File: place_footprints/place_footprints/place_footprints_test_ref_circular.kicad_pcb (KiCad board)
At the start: 2 copper layers, 64 parts

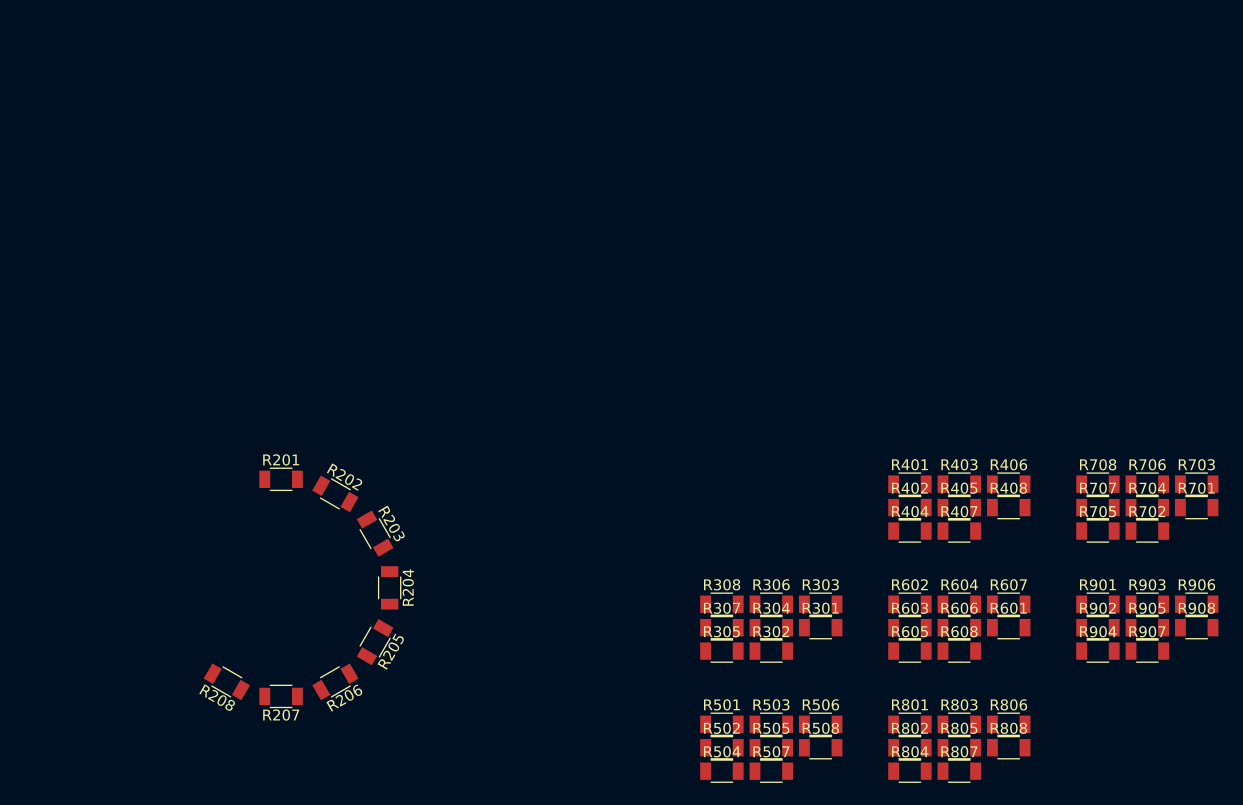
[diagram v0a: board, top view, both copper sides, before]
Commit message: Fixed circular placement
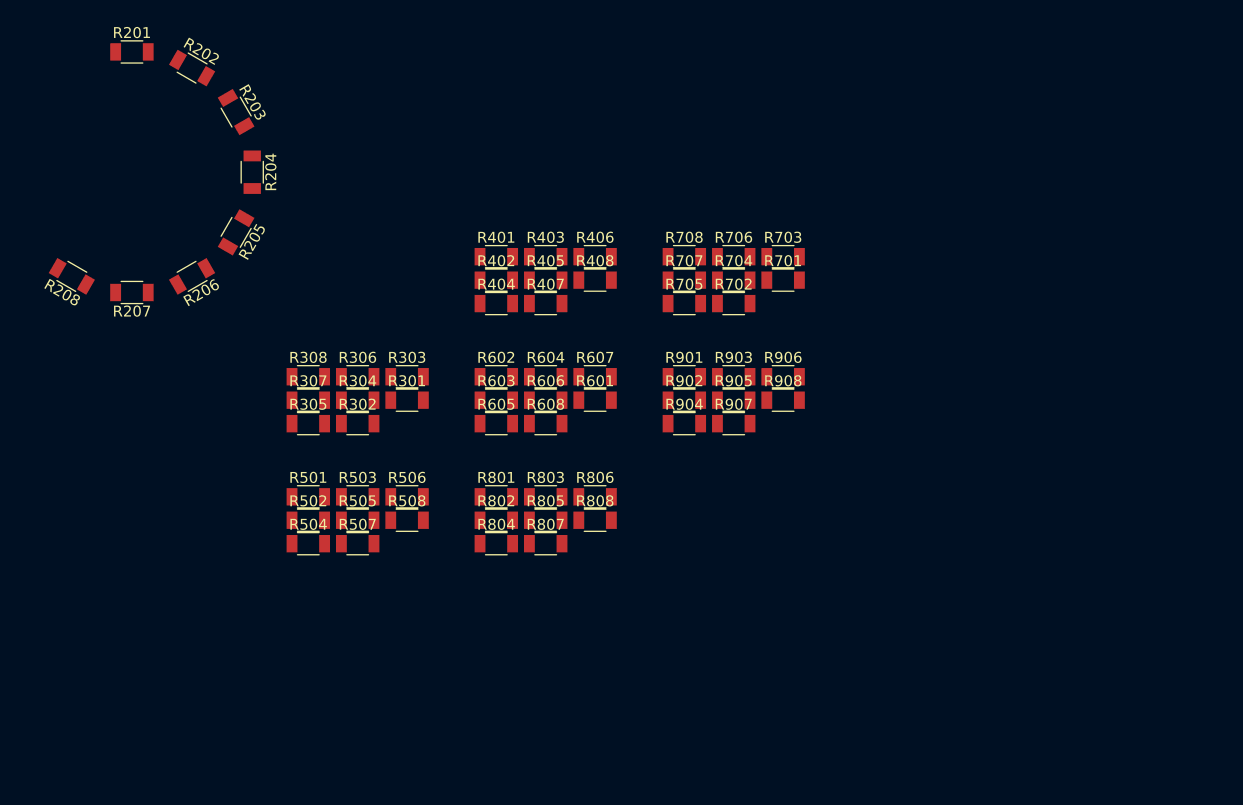
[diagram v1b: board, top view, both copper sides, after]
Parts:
- moved R301 43.5 mm to (69.2, 61.3)
- moved R302 43.5 mm to (64.6, 63.5)
- moved R303 43.5 mm to (69.2, 59.1)
- moved R304 43.5 mm to (64.6, 61.3)
- moved R306 43.5 mm to (64.6, 59.1)
- moved R401 43.5 mm to (77.4, 48.1)
- moved R402 43.5 mm to (77.4, 50.2)
- moved R404 43.5 mm to (77.4, 52.4)
- moved R503 43.5 mm to (64.6, 70.2)
- moved R505 43.5 mm to (64.6, 72.4)
- moved R506 43.5 mm to (69.2, 70.2)
- moved R507 43.5 mm to (64.6, 74.5)
- moved R508 43.5 mm to (69.2, 72.4)
- moved R602 43.5 mm to (77.4, 59.1)
- moved R603 43.5 mm to (77.4, 61.3)
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
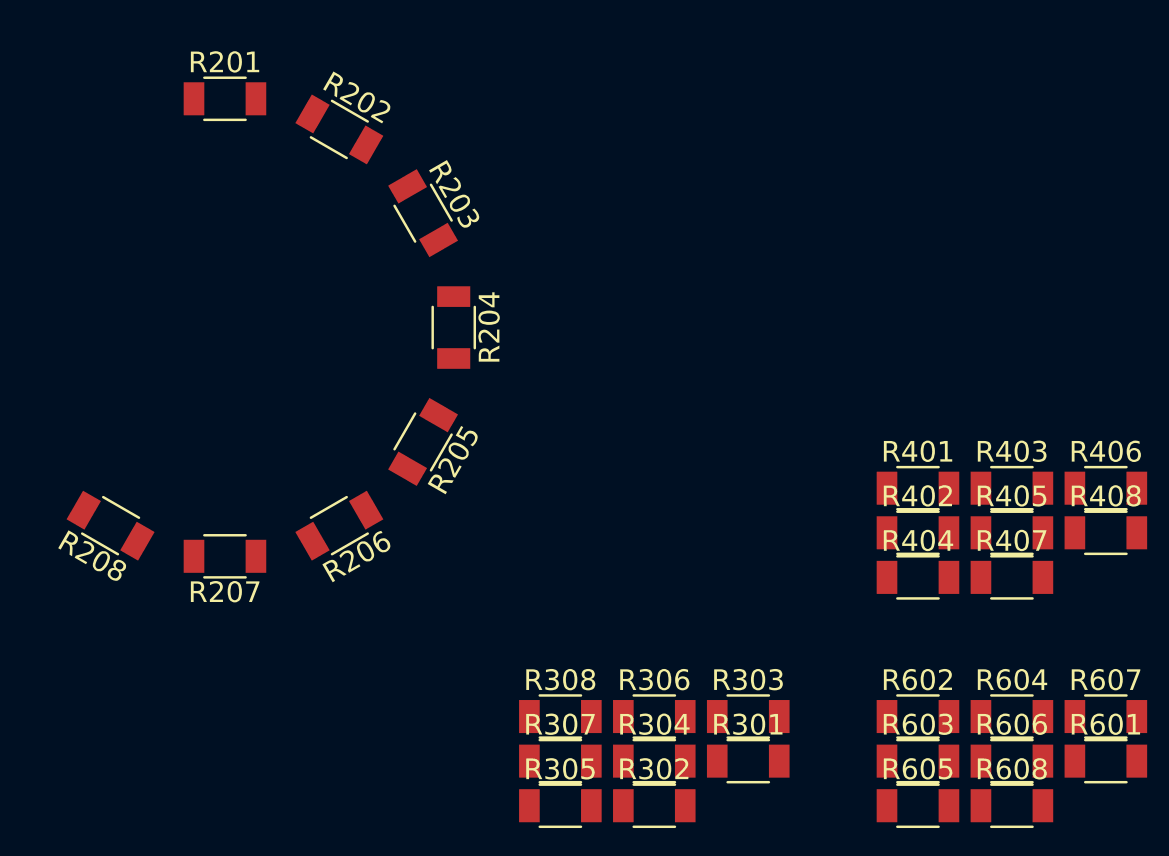
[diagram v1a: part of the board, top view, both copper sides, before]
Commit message: added support for any footprint to serve as a reference in linear and circular mode
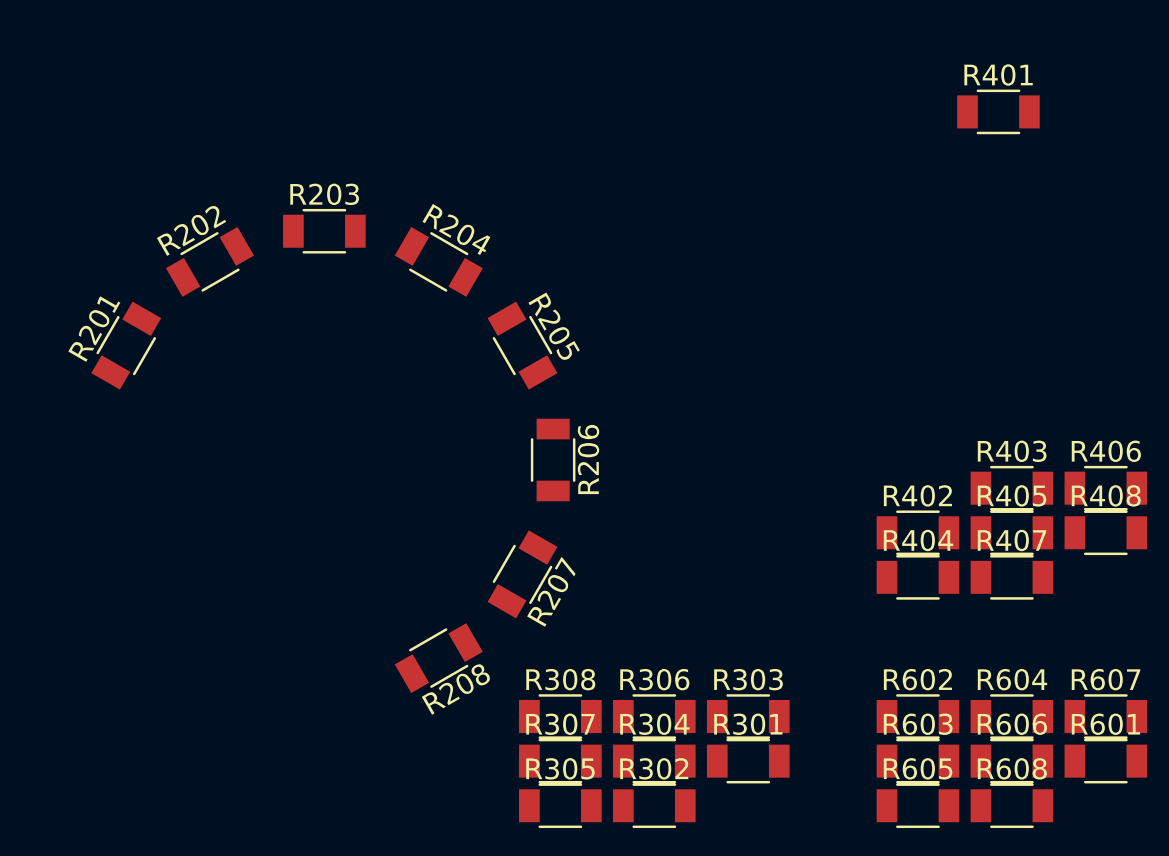
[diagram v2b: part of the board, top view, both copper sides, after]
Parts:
- moved R401 18.6 mm to (81.3, 29.8)
- moved R208 17.1 mm to (54.2, 56.3), turned to 210 degrees
- moved R207 14.4 mm to (58.2, 52.2), turned to 240 degrees
- moved R201 12.9 mm to (39.0, 41.2), turned to 60 degrees
- moved R206 10.8 mm to (59.7, 46.7), turned to 270 degrees
- moved R202 8.97 mm to (43.1, 37.1), turned to 30 degrees
- moved R205 6.70 mm to (58.2, 41.2), turned to 300 degrees
- moved R203 4.86 mm to (48.6, 35.6), turned to 0 degrees
- moved R204 3.26 mm to (54.2, 37.1), turned to 330 degrees

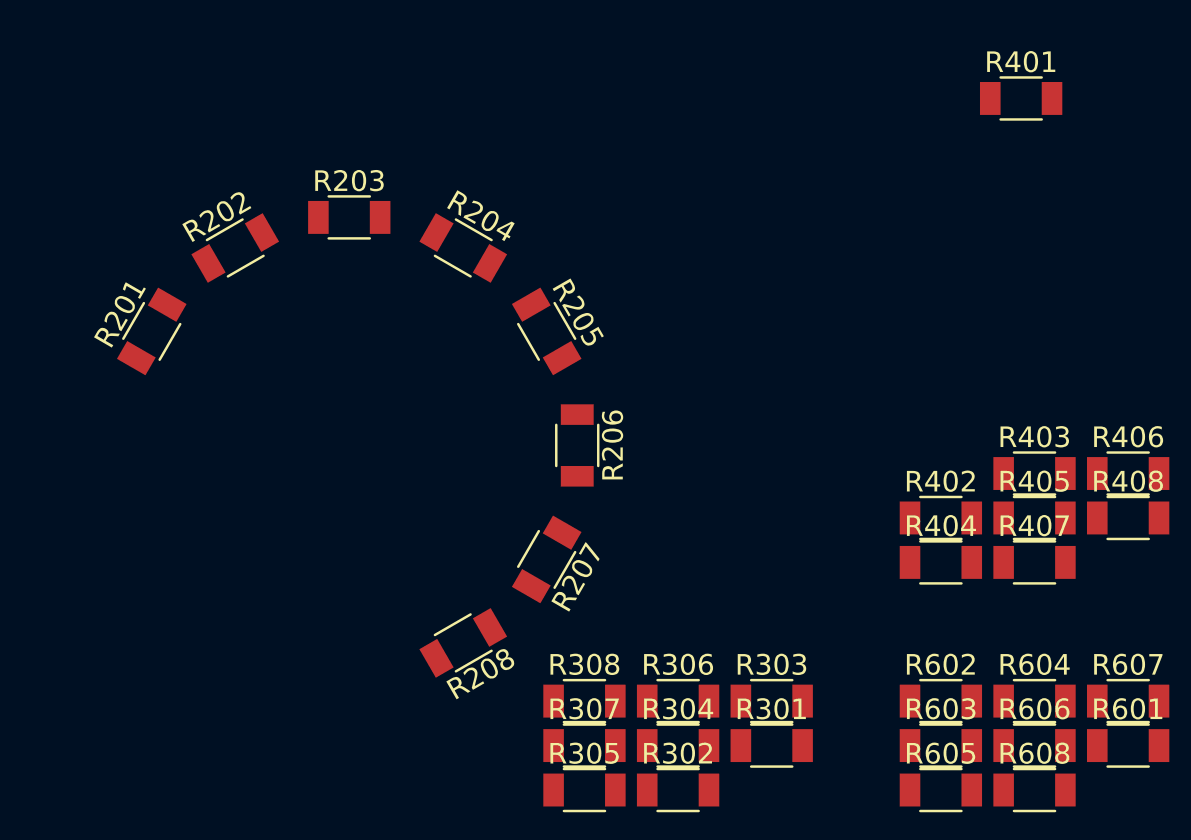
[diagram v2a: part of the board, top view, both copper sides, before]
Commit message: updated test cases
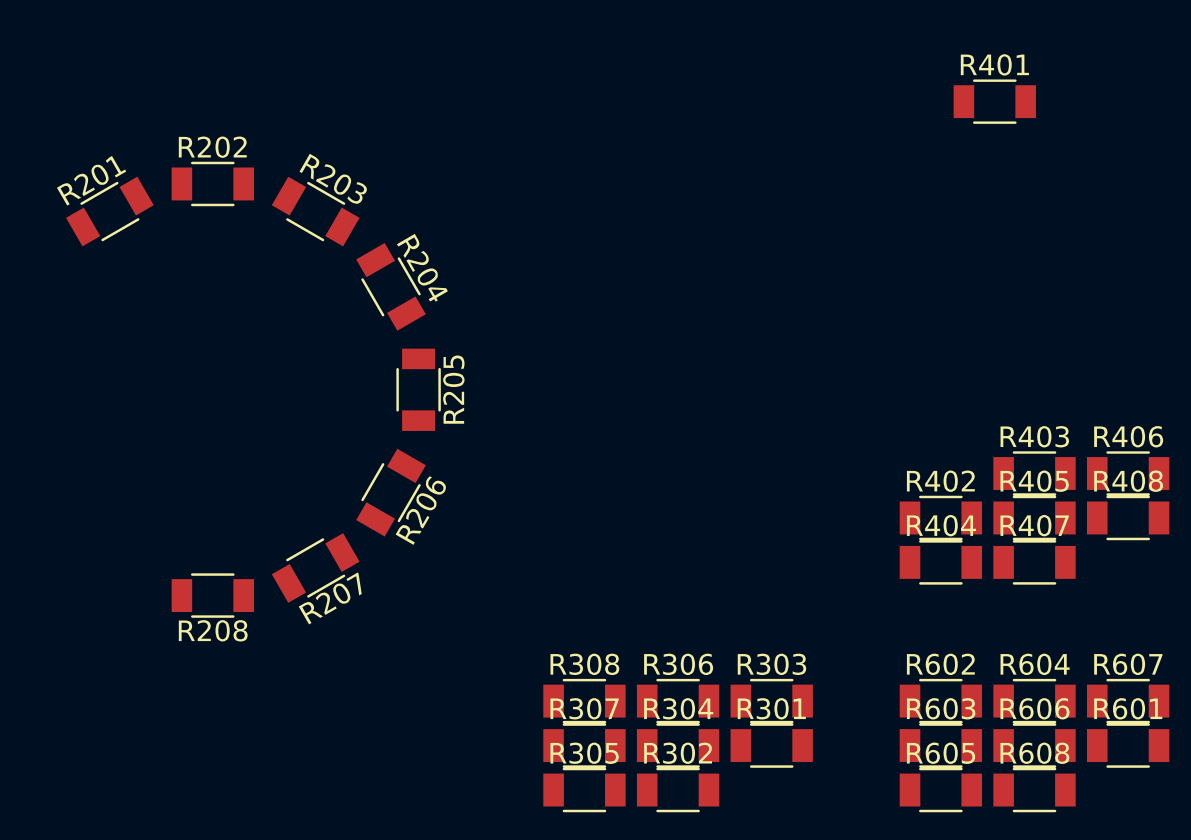
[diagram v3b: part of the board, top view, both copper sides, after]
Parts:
- moved R208 12.4 mm to (42.0, 54.0), turned to 180 degrees
- moved R207 11.2 mm to (47.0, 52.7), turned to 210 degrees
- moved R206 9.34 mm to (50.7, 49.0), turned to 240 degrees
- moved R205 6.84 mm to (52.0, 44.0), turned to 270 degrees
- moved R201 6.17 mm to (37.0, 35.3), turned to 30 degrees
- moved R204 3.99 mm to (50.7, 39.0), turned to 300 degrees
- moved R202 3.29 mm to (42.0, 34.0), turned to 0 degrees
- moved R203 1.65 mm to (47.0, 35.3), turned to 330 degrees
- moved R401 1.29 mm to (80.0, 30.0)
